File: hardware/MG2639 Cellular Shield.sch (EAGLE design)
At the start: 63 parts, among them Q1 MMBT2222A, U1 SPX29302, U2 TXB0104, U3 MG2639V3

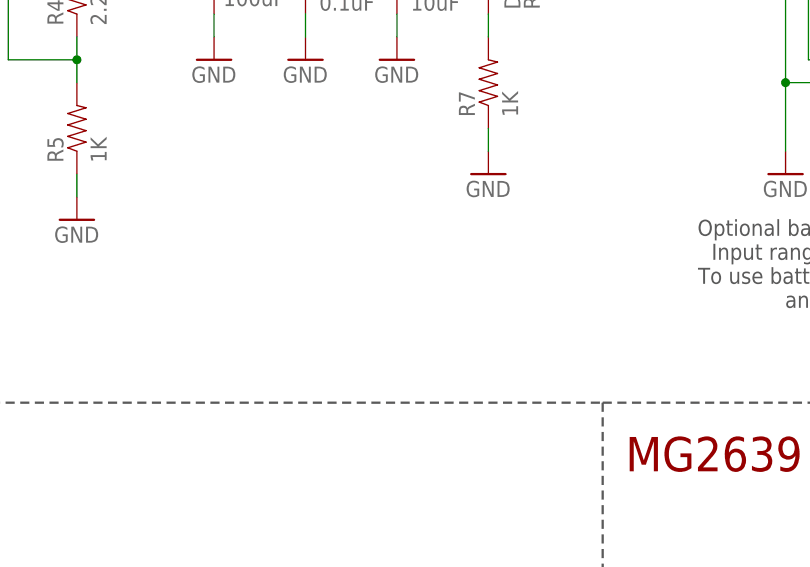
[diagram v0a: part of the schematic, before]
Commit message: Adding test point to 3.8V bus.
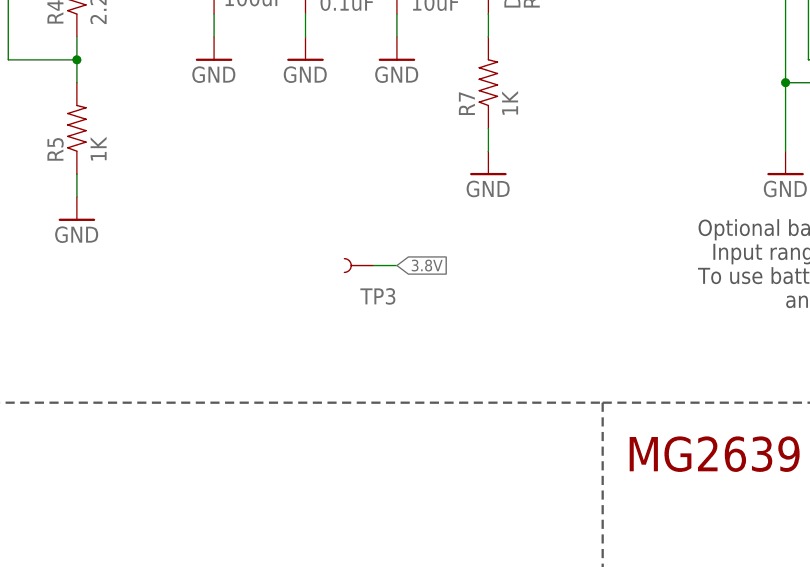
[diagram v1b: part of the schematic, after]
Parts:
- added TP3: TEST-POINT3X5, SparkFun-Passives:TEST-POINT3X5
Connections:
- net 3.8V: now also TP3.1
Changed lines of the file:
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@@
 <part name="SJ9" library="SparkFun-Passives" deviceset="JUMPER-PAD-3-2OF3_NC_BY_TRACE" device="" value=""/>
 <part name="SJ10" library="SparkFun-Passives" deviceset="JUMPER-PAD-3-2OF3_NC_BY_TRACE" device="" value=""/>
+<part name="TP3" library="SparkFun-Passives" deviceset="TEST-POINT" device="3X5" value=""/>
 </parts>
 <sheets>
@@
 <instance part="SJ9" gate="G$1" x="327.66" y="218.44"/>
 <instance part="SJ10" gate="G$1" x="327.66" y="238.76"/>
+<instance part="TP3" gate="G$1" x="109.22" y="205.74" rot="R180"/>
 </instances>
 <busses>
@@
 <junction x="124.46" y="243.84"/>
 </segment>
-</net>
+<segment>
+<pinref part="TP3" gate="G$1" pin="1"/>
+<wire x1="109.22" y1="205.74" x2="111.76" y2="205.74" width="0.1524" layer="91"/>
+<label x="111.76" y="205.74" size="1.27" layer="95" xref="yes"/>
+</segment>
+</net>

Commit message: Re-routing GTX-HV to D8 on the Arduino.
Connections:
- removed net CELL_RESET: JP3.*D6
- removed net JP9: JP3.D8
- net GTX-SOFT: now also JP3.D8
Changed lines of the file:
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@@
-</segment>
-</net>
-<net name="CELL_RESET" class="0">
-<segment>
-<pinref part="JP3" gate="G$1" pin="*D6"/>
-<wire x1="378.46" y1="236.22" x2="375.92" y2="236.22" width="0.1524" layer="91"/>
-<label x="375.92" y="236.22" size="1.27" layer="95" rot="MR0" xref="yes"/>
 </segment>
 </net>
@@
 <label x="330.2" y="210.82" size="1.27" layer="95" xref="yes"/>
 </segment>
+<segment>
+<pinref part="JP3" gate="G$1" pin="D8"/>
+<wire x1="378.46" y1="231.14" x2="375.92" y2="231.14" width="0.1524" layer="91"/>
+<label x="375.92" y="231.14" size="1.27" layer="95" rot="R180" xref="yes"/>
+</segment>
 </net>
 <net name="GRX-SOFT" class="0">
@@
 </segment>
 </net>
-<net name="JP9" class="0">
-<segment>
-<pinref part="JP3" gate="G$1" pin="D8"/>
-<wire x1="378.46" y1="231.14" x2="375.92" y2="231.14" width="0.1524" layer="91"/>
-<label x="375.92" y="231.14" size="1.27" layer="95" rot="R180" xref="yes"/>
-</segment>
-</net>

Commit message: Cleaning up nets around Arduino Shield connector (removing stubs).
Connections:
- removed net A1: JP3.A1
- removed net A2: JP3.A2
- removed net A3: JP3.A3
- removed net A4: JP3.A4
- removed net A5: JP3.A5
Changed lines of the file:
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@@
-</segment>
-</net>
-<net name="A1" class="0">
-<segment>
-<wire x1="403.86" y1="251.46" x2="406.4" y2="251.46" width="0.1524" layer="91"/>
-<pinref part="JP3" gate="G$1" pin="A1"/>
-<label x="406.4" y="251.46" size="1.27" layer="95" rot="MR180" xref="yes"/>
-</segment>
-</net>
-<net name="A2" class="0">
-<segment>
-<wire x1="403.86" y1="248.92" x2="406.4" y2="248.92" width="0.1524" layer="91"/>
-<pinref part="JP3" gate="G$1" pin="A2"/>
-<label x="406.4" y="248.92" size="1.27" layer="95" rot="MR180" xref="yes"/>
-</segment>
-</net>
-<net name="A3" class="0">
-<segment>
-<wire x1="403.86" y1="246.38" x2="406.4" y2="246.38" width="0.1524" layer="91"/>
-<pinref part="JP3" gate="G$1" pin="A3"/>
-<label x="406.4" y="246.38" size="1.27" layer="95" rot="MR180" xref="yes"/>
-</segment>
-</net>
-<net name="A4" class="0">
-<segment>
-<wire x1="403.86" y1="243.84" x2="406.4" y2="243.84" width="0.1524" layer="91"/>
-<pinref part="JP3" gate="G$1" pin="A4"/>
-<label x="406.4" y="243.84" size="1.27" layer="95" rot="MR180" xref="yes"/>
-</segment>
-</net>
-<net name="A5" class="0">
-<segment>
-<wire x1="403.86" y1="241.3" x2="406.4" y2="241.3" width="0.1524" layer="91"/>
-<pinref part="JP3" gate="G$1" pin="A5"/>
-<label x="406.4" y="241.3" size="1.27" layer="95" rot="MR180" xref="yes"/>
 </segment>
 </net>

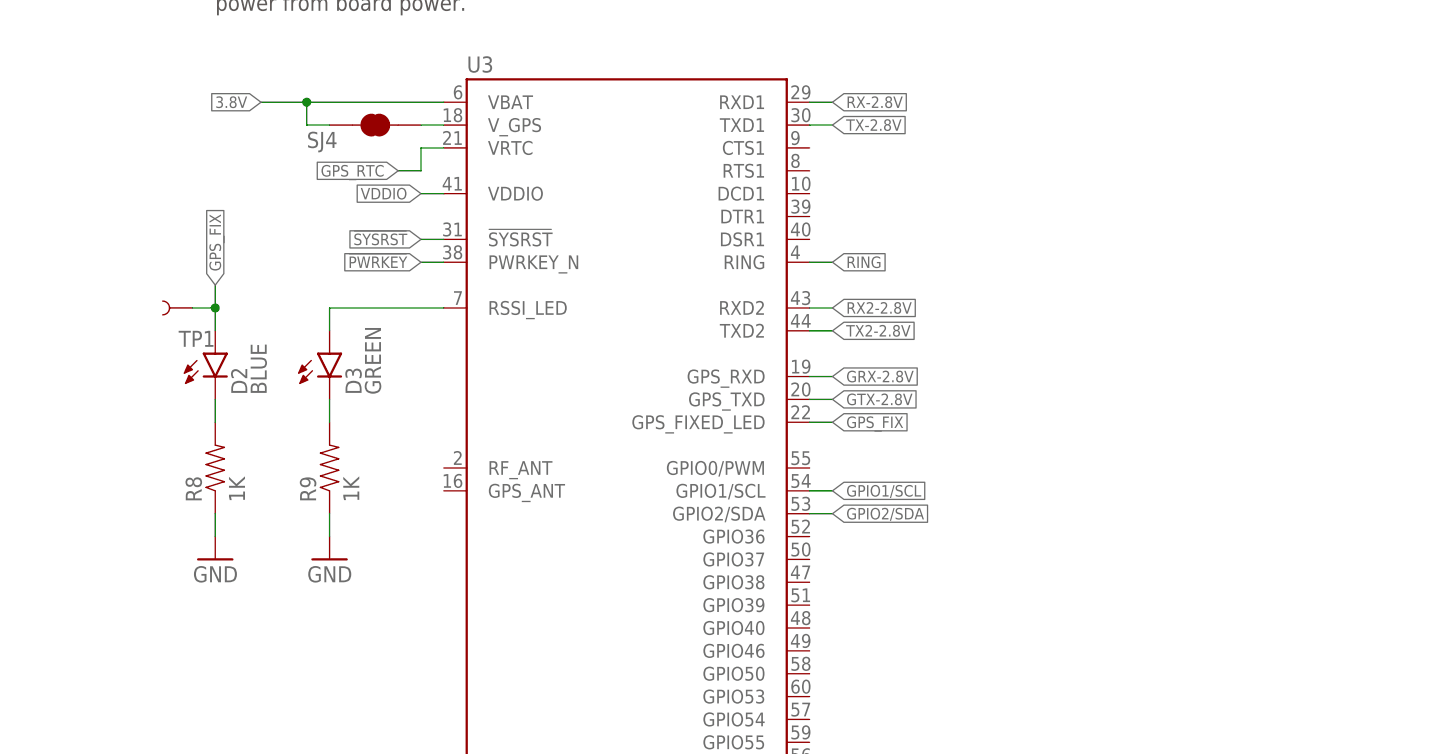
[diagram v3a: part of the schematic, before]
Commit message: Switching GPS fix indicator LED to yellow.
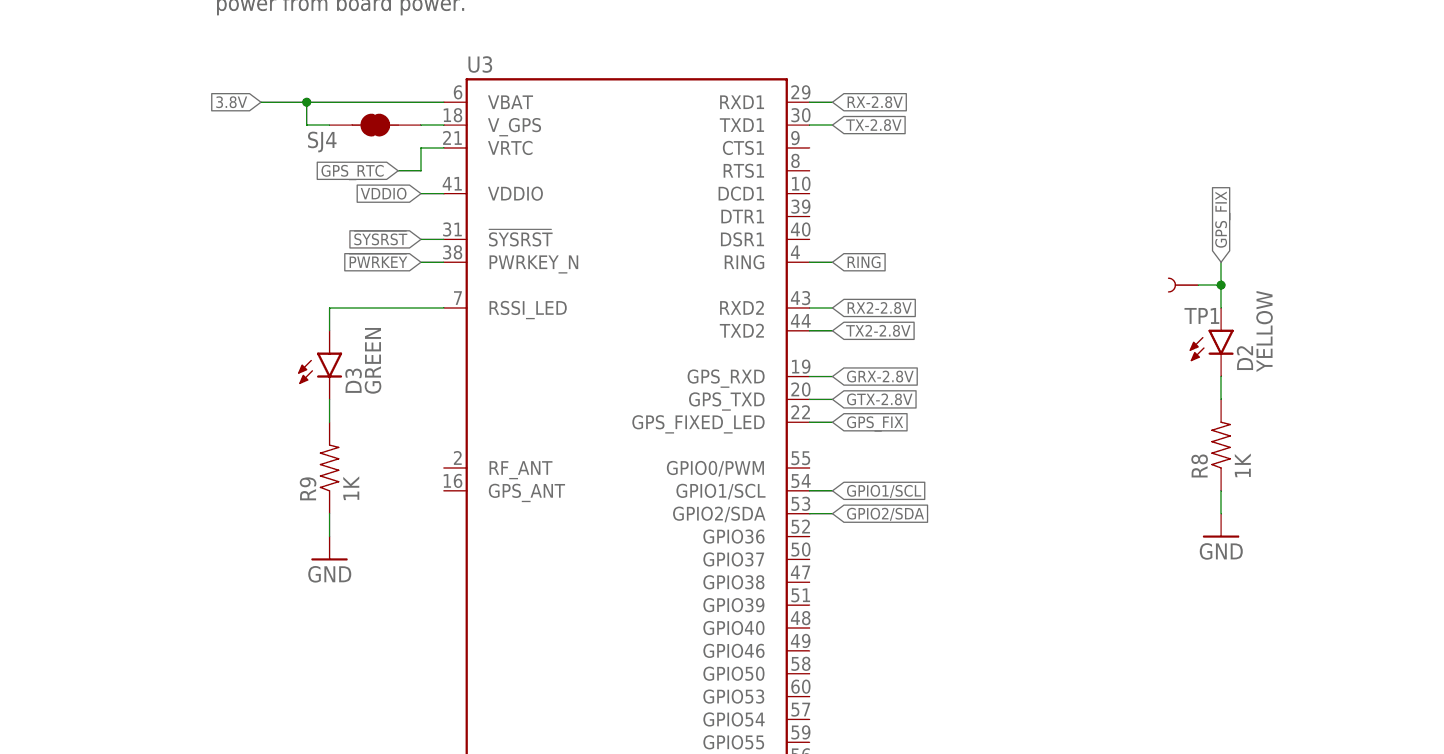
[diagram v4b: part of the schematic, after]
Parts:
- D2: value BLUE -> YELLOW; device SparkFun-LED:LED-BLUE1206 -> SparkFun-LED:LED-YELLOWLARGE
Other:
- moved on the sheet: D2, R8, TP1
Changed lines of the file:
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@@
 <part name="R9" library="SparkFun-Resistors" deviceset="1KOHM1/10W1%(0603)" device="" value="1K"/>
 <part name="GND19" library="SparkFun" deviceset="GND" device=""/>
-<part name="D2" library="SparkFun-LED" deviceset="LED-BLUE" device="1206" value="BLUE"/>
 <part name="R8" library="SparkFun-Resistors" deviceset="1KOHM1/10W1%(0603)" device="" value="1K"/>
 <part name="GND18" library="SparkFun" deviceset="GND" device=""/>
@@
 <part name="SJ10" library="SparkFun-Passives" deviceset="JUMPER-PAD-3-2OF3_NC_BY_TRACE" device="" value=""/>
 <part name="TP3" library="SparkFun-Passives" deviceset="TEST-POINT" device="3X5" value=""/>
+<part name="D2" library="SparkFun-LED" deviceset="LED-YELLOW" device="LARGE" value="YELLOW"/>
 </parts>
 <sheets>
@@
 <instance part="R9" gate="G$1" x="187.96" y="106.68" rot="R90"/>
 <instance part="GND19" gate="1" x="187.96" y="96.52" rot="MR0"/>
-<instance part="D2" gate="G$1" x="175.26" y="119.38"/>
-<instance part="R8" gate="G$1" x="175.26" y="106.68" rot="R90"/>
-<instance part="GND18" gate="1" x="175.26" y="96.52" rot="MR0"/>
+<instance part="R8" gate="G$1" x="287.02" y="109.22" rot="R90"/>
+<instance part="GND18" gate="1" x="287.02" y="99.06" rot="MR0"/>
 <instance part="C5" gate="G$1" x="99.06" y="71.12"/>
 <instance part="C4" gate="G$1" x="88.9" y="71.12"/>
@@
 <instance part="GND22" gate="1" x="218.44" y="195.58" rot="MR0"/>
 <instance part="JP2" gate="G$1" x="167.64" y="226.06" rot="MR0"/>
-<instance part="TP1" gate="G$1" x="172.72" y="124.46" rot="R180"/>
+<instance part="TP1" gate="G$1" x="284.48" y="127" rot="R180"/>
 <instance part="TP2" gate="G$1" x="81.28" y="30.48" rot="MR180"/>
 <instance part="STANDOFF4" gate="G$1" x="429.26" y="25.4"/>
@@
 <instance part="SJ10" gate="G$1" x="327.66" y="238.76"/>
 <instance part="TP3" gate="G$1" x="109.22" y="205.74" rot="R180"/>
+<instance part="D2" gate="G$1" x="287.02" y="121.92"/>
 </instances>
 <busses>
@@
 <pinref part="R8" gate="G$1" pin="1"/>
 <pinref part="GND18" gate="1" pin="GND"/>
-<wire x1="175.26" y1="99.06" x2="175.26" y2="101.6" width="0.1524" layer="91"/>
+<wire x1="287.02" y1="101.6" x2="287.02" y2="104.14" width="0.1524" layer="91"/>
 </segment>
 <segment>
@@
 </segment>
 <segment>
+<wire x1="287.02" y1="124.46" x2="287.02" y2="127" width="0.1524" layer="91"/>
+<label x="287.02" y="129.54" size="1.27" layer="95" rot="R90" xref="yes"/>
+<pinref part="TP1" gate="G$1" pin="1"/>
+<wire x1="287.02" y1="127" x2="287.02" y2="129.54" width="0.1524" layer="91"/>
+<wire x1="284.48" y1="127" x2="287.02" y2="127" width="0.1524" layer="91"/>
+<junction x="287.02" y="127"/>
 <pinref part="D2" gate="G$1" pin="A"/>
-<wire x1="175.26" y1="121.92" x2="175.26" y2="124.46" width="0.1524" layer="91"/>
-<label x="175.26" y="127" size="1.27" layer="95" rot="R90" xref="yes"/>
-<pinref part="TP1" gate="G$1" pin="1"/>
-<wire x1="175.26" y1="124.46" x2="175.26" y2="127" width="0.1524" layer="91"/>
-<wire x1="172.72" y1="124.46" x2="175.26" y2="124.46" width="0.1524" layer="91"/>
-<junction x="175.26" y="124.46"/>
 </segment>
 </net>
@@
 <segment>
 <pinref part="R8" gate="G$1" pin="2"/>
+<wire x1="287.02" y1="116.84" x2="287.02" y2="114.3" width="0.1524" layer="91"/>
 <pinref part="D2" gate="G$1" pin="C"/>
-<wire x1="175.26" y1="114.3" x2="175.26" y2="111.76" width="0.1524" layer="91"/>
-</segment>
-</net>
+</segment>
+</net>
